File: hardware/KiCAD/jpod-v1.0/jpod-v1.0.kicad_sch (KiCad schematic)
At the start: 29 parts, among them J1 SD_Card, J2 SPI_DEBUG, J3 LCD_HEADER, Q1 AO3400A, U1 ESP32

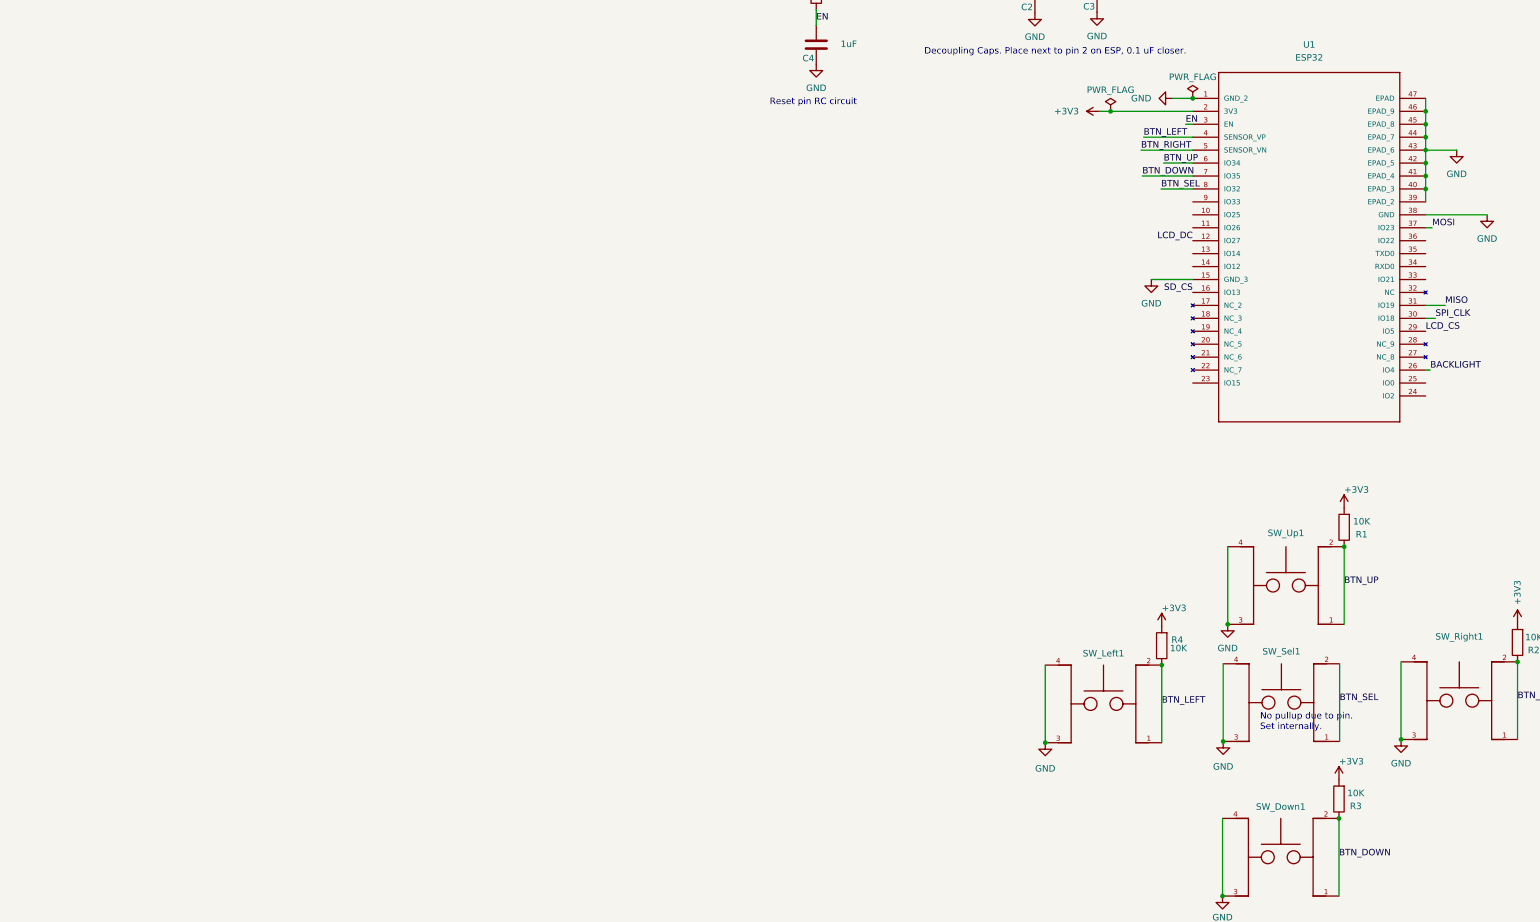
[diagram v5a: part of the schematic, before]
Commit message: sch finished with DAC and 3.5mm jack
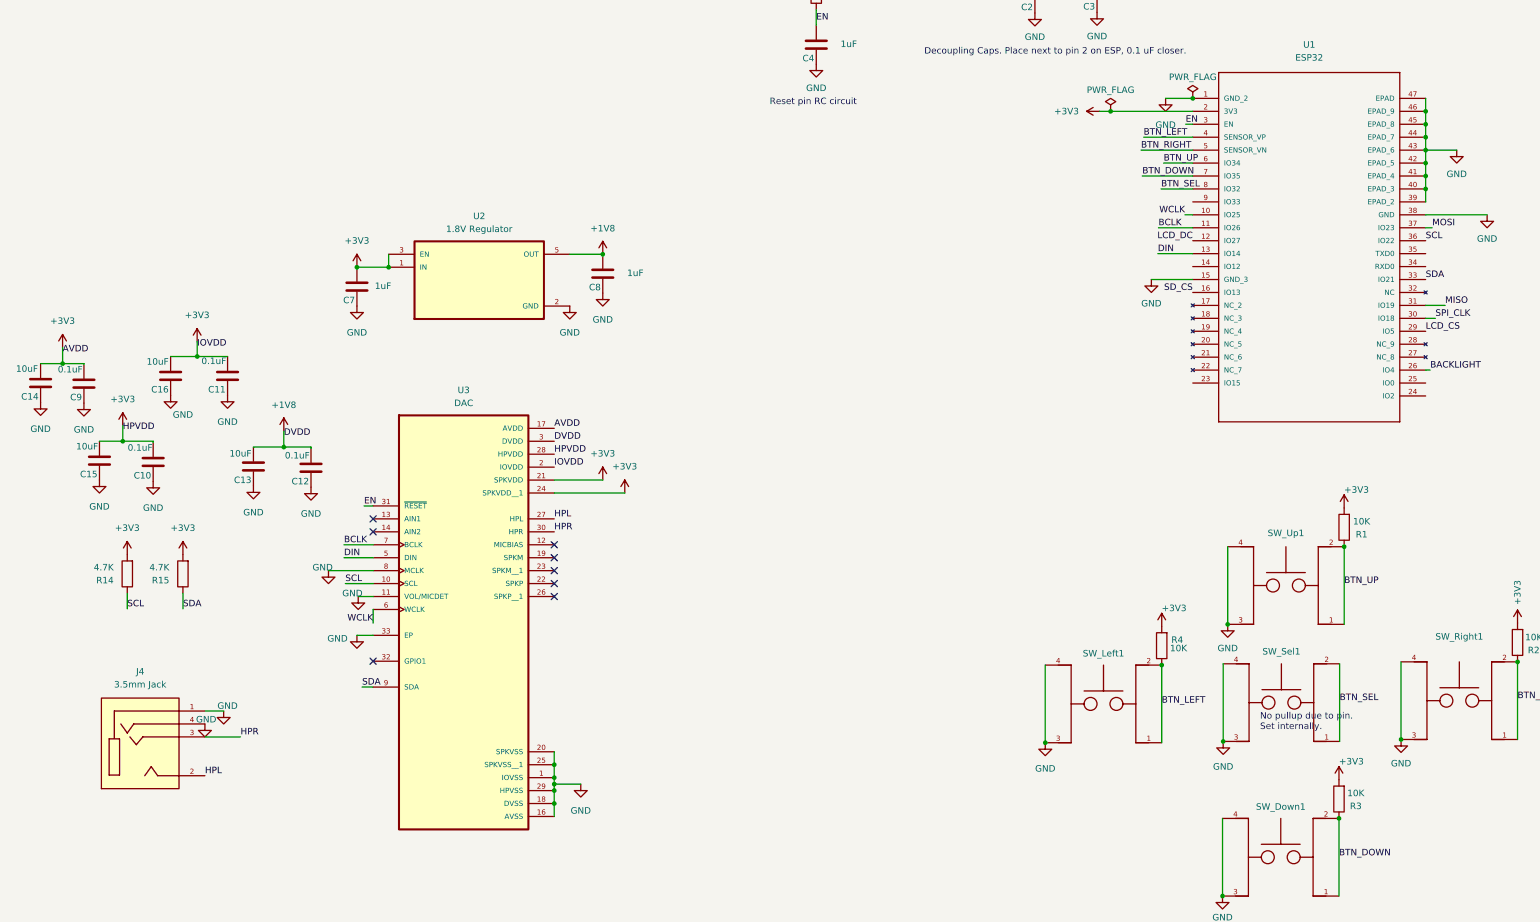
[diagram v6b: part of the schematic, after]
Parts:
- added C10, C11, C12, C9: 0.1uF, Capacitor_SMD:C_0603_1608Metric, symbol Device:C
- added C13, C14, C15, C16: 10uF, Capacitor_SMD:C_0603_1608Metric, symbol Device:C
- added C7, C8: 1uF, Capacitor_SMD:C_0603_1608Metric, symbol Device:C
- added J4: 3.5mm Jack, SJ-43514-SMT-TR:CUI_SJ-43514-SMT-TR, symbol jpod:SJ-43514-SMT-TR
- added R14, R15: 4.7K, Resistor_SMD:R_0603_1608Metric, symbol Device:R
- added U2: 1.8V Regulator, TLV75518PDBVR:SOT95P280X145-5N, symbol jpod:TLV75518PDBVR
- added U3: DAC, jpod_footprints:TLV320DAC3100IRHBT, symbol jpod:TLV320DAC3100IRHBT
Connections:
- net +3V3: now also C10.2, C11.2, C14.2, C15.2, C16.2, C7.2, C9.2, R14.2, R15.2, U2.1 (IN), U2.3 (EN), U3.17 (AVDD), U3.2 (IOVDD), U3.21 (SPKVDD), U3.24 (SPKVDD__1), U3.28 (HPVDD)
- net EN: now also U3.31 (~{RESET})
- net GND: now also C10.1, C11.1, C12.1, C13.1, C14.1, C15.1, C16.1, C7.1, C8.1, C9.1, J4.1, J4.4, U2.2 (GND), U3.1 (IOVSS), U3.11 (VOL/MICDET), U3.16 (AVSS), U3.18 (DVSS), U3.20 (SPKVSS), U3.25 (SPKVSS__1), U3.29 (HPVSS), U3.33 (EP), U3.8 (MCLK)
- net WCLK: now reaches U1.10 (IO25)
- net WCLK: now also U3.6 (WCLK)
- net BCLK: now reaches U1.11 (IO26)
- net BCLK: now also U3.7 (BCLK)
- net DIN: now reaches U1.13 (IO14)
- net DIN: now also U3.5 (DIN)
- net SDA: now reaches U1.33 (IO21)
- net SDA: now also R15.1, U3.9 (SDA)
- net SCL: now reaches U1.36 (IO22)
- net SCL: now also R14.1, U3.10 (SCL)
- new net +1V8: C12.2, C13.2, C8.2, U2.5 (OUT), U3.3 (DVDD)
- new net HPL: J4.2, U3.27 (HPL)
- new net HPR: J4.3, U3.30 (HPR)
- no-connect marks 3 -> 11

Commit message: schematic warning cleanup. usb-C and lipo battery still left todo
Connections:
- net PLACEHOLDER_LCD_CS is gone; now on net LCD_CS: J2.5 (Pin_5)
- net PLACEHOLDER_LCD_DC is gone; now on net LCD_DC: J2.6 (Pin_6)
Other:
- moved on the sheet: C4, R10
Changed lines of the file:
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@@
     (stroke (width 0) (type default))
   )
-  (wire (pts (xy 194.818 104.394) (xy 194.818 107.442))
+  (wire (pts (xy 202.057 104.394) (xy 202.057 107.442))
     (stroke (width 0) (type default))
   )
@@
     (stroke (width 0) (type default))
   )
+  (wire (pts (xy 158.115 189.103) (xy 143.383 189.103))
+    (stroke (width 0) (type default))
+  )
   (wire (pts (xy 278.765 55.499) (xy 278.765 56.769))
     (stroke (width 0) (type default))
@@
     (stroke (width 0) (type default))
   )
-  (wire (pts (xy 90.297 190.246) (xy 90.297 187.071))
+  (wire (pts (xy 90.297 181.483) (xy 90.297 190.246))
     (stroke (width 0) (type default))
   )
@@
     (effects (font (size 1.27 1.27)) (justify left bottom))
   )
-  (text "Reset pin RC circuit\n" (at 185.674 123.317 0)
+  (text "Reset pin RC circuit\n" (at 192.913 123.317 0)
     (effects (font (size 1.27 1.27)) (justify left bottom))
   )
@@
     (effects (font (size 1.27 1.27)) (justify right bottom))
   )
-  (label "PLACEHOLDER_LCD_CS" (at 454.533 34.163 0) (fields_autoplaced)
+  (label "LCD_CS" (at 454.533 34.163 0) (fields_autoplaced)
     (effects (font (size 1.27 1.27)) (justify left bottom))
   )
@@
     (effects (font (size 1.27 1.27)) (justify left bottom))
   )
-  (label "EN" (at 194.818 106.807 0) (fields_autoplaced)
+  (label "EN" (at 202.057 106.807 0) (fields_autoplaced)
     (effects (font (size 1.27 1.27)) (justify left bottom))
   )
-  (label "PLACEHOLDER_LCD_DC" (at 454.533 36.703 0) (fields_autoplaced)
+  (label "LCD_DC" (at 454.533 36.703 0) (fields_autoplaced)
     (effects (font (size 1.27 1.27)) (justify left bottom))
   )
@@
     (effects (font (size 1.27 1.27)) (justify left bottom))
   )
-  (label "DVDD" (at 90.297 188.341 0) (fields_autoplaced)
-    (effects (font (size 1.27 1.27)) (justify left bottom))
-  )
   (label "BTN_RIGHT" (at 258.572 131.953 0) (fields_autoplaced)
     (effects (font (size 1.27 1.27)) (justify left bottom))
@@
     (effects (font (size 1.27 1.27)) (justify left bottom))
   )
-  (label "DVDD" (at 143.383 189.103 0) (fields_autoplaced)
-    (effects (font (size 1.27 1.27)) (justify left bottom))
-  )
   (label "BTN_LEFT" (at 262.636 240.919 0) (fields_autoplaced)
     (effects (font (size 1.27 1.27)) (justify left bottom))
@@
     )
   )
-  (symbol (lib_id "power:+1V8") (at 90.297 187.071 0) (unit 1)
+  (symbol (lib_id "power:+1V8") (at 90.297 181.483 0) (unit 1)
     (in_bom yes) (on_board yes) (dnp no) (fields_autoplaced)
-    (property "Reference" "#PWR054" (at 90.297 190.881 0)
+    (property "Reference" "#PWR054" (at 90.297 185.293 0)
       (effects (font (size 1.27 1.27)) hide)
     )
-    (property "Value" "+1V8" (at 90.297 181.991 0)
+    (property "Value" "+1V8" (at 90.297 176.403 0)
       (effects (font (size 1.27 1.27)))
     )
-    (property "Footprint" "" (at 90.297 187.071 0)
+    (property "Footprint" "" (at 90.297 181.483 0)
       (effects (font (size 1.27 1.27)) hide)
     )
-    (property "Datasheet" "" (at 90.297 187.071 0)
+    (property "Datasheet" "" (at 90.297 181.483 0)
       (effects (font (size 1.27 1.27)) hide)
     )
@@
     )
   )
-  (symbol (lib_id "Device:R") (at 194.818 100.584 180) (unit 1)
+  (symbol (lib_id "Device:R") (at 202.057 100.584 180) (unit 1)
     (in_bom yes) (on_board yes) (dnp no) (fields_autoplaced)
-    (property "Reference" "R10" (at 192.151 101.854 0)
+    (property "Reference" "R10" (at 199.39 101.854 0)
       (effects (font (size 1.27 1.27)) (justify left))
     )
-    (property "Value" "10K" (at 192.151 99.314 0)
+    (property "Value" "10K" (at 199.39 99.314 0)
       (effects (font (size 1.27 1.27)) (justify left))
     )
-    (property "Footprint" "Resistor_SMD:R_0603_1608Metric" (at 196.596 100.584 90)
+    (property "Footprint" "Resistor_SMD:R_0603_1608Metric" (at 203.835 100.584 90)
       (effects (font (size 1.27 1.27)) hide)
     )
-    (property "Datasheet" "~" (at 194.818 100.584 0)
+    (property "Datasheet" "~" (at 202.057 100.584 0)
       (effects (font (size 1.27 1.27)) hide)
     )
@@
     )
   )
+  (symbol (lib_id "power:+1V8") (at 158.115 189.103 0) (unit 1)
+    (in_bom yes) (on_board yes) (dnp no) (fields_autoplaced)
+    (property "Reference" "#PWR069" (at 158.115 192.913 0)
+      (effects (font (size 1.27 1.27)) hide)
+    )
+    (property "Value" "+1V8" (at 158.115 184.023 0)
+      (effects (font (size 1.27 1.27)))
+    )
+    (property "Footprint" "" (at 158.115 189.103 0)
+      (effects (font (size 1.27 1.27)) hide)
+    )
+    (property "Datasheet" "" (at 158.115 189.103 0)
+      (effects (font (size 1.27 1.27)) hide)
+    )
+    (pin "1")
+    (instances
+      (project "jpod-v1.0"
+        (path "/6f39d746-fc34-453f-ad9d-f86b2a09a03d"
+          (reference "#PWR069") (unit 1)
+        )
+      )
+    )
+  )
   (symbol (lib_id "power:GND") (at 424.434 95.631 0) (unit 1)
     (in_bom yes) (on_board yes) (dnp no) (fields_autoplaced)
@@
     )
   )
-  (symbol (lib_id "power:GND") (at 194.818 115.062 0) (unit 1)
+  (symbol (lib_id "power:GND") (at 202.057 115.062 0) (unit 1)
     (in_bom yes) (on_board yes) (dnp no) (fields_autoplaced)
-    (property "Reference" "#PWR030" (at 194.818 121.412 0)
+    (property "Reference" "#PWR030" (at 202.057 121.412 0)
       (effects (font (size 1.27 1.27)) hide)
     )
-    (property "Value" "GND" (at 194.818 119.761 0)
+    (property "Value" "GND" (at 202.057 119.761 0)
       (effects (font (size 1.27 1.27)))
     )
-    (property "Footprint" "" (at 194.818 115.062 0)
+    (property "Footprint" "" (at 202.057 115.062 0)
       (effects (font (size 1.27 1.27)) hide)
     )
-    (property "Datasheet" "" (at 194.818 115.062 0)
+    (property "Datasheet" "" (at 202.057 115.062 0)
       (effects (font (size 1.27 1.27)) hide)
     )
@@
     )
   )
-  (symbol (lib_id "Device:C") (at 194.818 111.252 180) (unit 1)
+  (symbol (lib_id "Device:C") (at 202.057 111.252 180) (unit 1)
     (in_bom yes) (on_board yes) (dnp no)
-    (property "Reference" "C4" (at 194.437 113.919 0)
+    (property "Reference" "C4" (at 201.676 113.919 0)
       (effects (font (size 1.27 1.27)) (justify left))
     )
-    (property "Value" "1uF" (at 202.819 111.125 0)
+    (property "Value" "1uF" (at 210.058 111.125 0)
       (effects (font (size 1.27 1.27)) (justify left))
     )
-    (property "Footprint" "Capacitor_SMD:C_0603_1608Metric" (at 193.8528 107.442 0)
+    (property "Footprint" "Capacitor_SMD:C_0603_1608Metric" (at 201.0918 107.442 0)
       (effects (font (size 1.27 1.27)) hide)
     )
-    (property "Datasheet" "~" (at 194.818 111.252 0)
+    (property "Datasheet" "~" (at 202.057 111.252 0)
       (effects (font (size 1.27 1.27)) hide)
     )
@@
     )
   )
-  (symbol (lib_id "power:+3V3") (at 194.818 96.774 0) (unit 1)
+  (symbol (lib_id "power:+3V3") (at 202.057 96.774 0) (unit 1)
     (in_bom yes) (on_board yes) (dnp no) (fields_autoplaced)
-    (property "Reference" "#PWR023" (at 194.818 100.584 0)
+    (property "Reference" "#PWR023" (at 202.057 100.584 0)
       (effects (font (size 1.27 1.27)) hide)
     )
-    (property "Value" "+3V3" (at 194.818 91.567 0)
+    (property "Value" "+3V3" (at 202.057 91.567 0)
       (effects (font (size 1.27 1.27)))
     )
-    (property "Footprint" "" (at 194.818 96.774 0)
+    (property "Footprint" "" (at 202.057 96.774 0)
       (effects (font (size 1.27 1.27)) hide)
     )
-    (property "Datasheet" "" (at 194.818 96.774 0)
+    (property "Datasheet" "" (at 202.057 96.774 0)
       (effects (font (size 1.27 1.27)) hide)
     )

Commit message: add lipo charger, buck boost, fuel gauge, updated hardware parts
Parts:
- added U4: Charger, jpod_footprints:BQ24075RGTR, symbol jpod:BQ24075RGTR
- added U5: Buck Boost, TPS63020DSJT:IC_TPS63020DSJT, symbol jpod:TPS63020DSJT
- added U6: Fuel Gauge, MAX17048G_T10:SON50P200X200X80-9N, symbol jpod:MAX17048G_T10
